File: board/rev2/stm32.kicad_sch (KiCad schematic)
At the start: 6 parts, among them U6 STM32G071CBUx

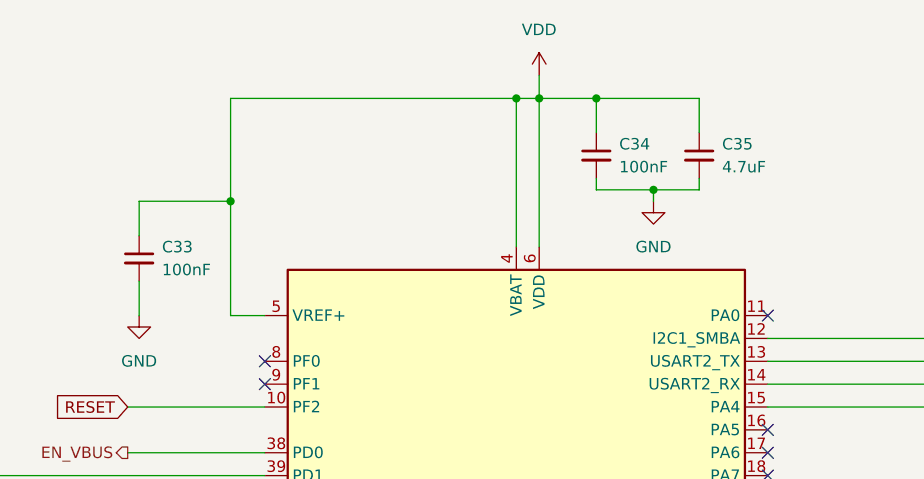
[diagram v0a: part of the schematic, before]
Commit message: Start board
add a few extra bypass caps too, and swap some pins on the USB mux

i forgot to add a bypass cap on the tpd6s so that also needs to happen

truly 63 capacitors is not enough
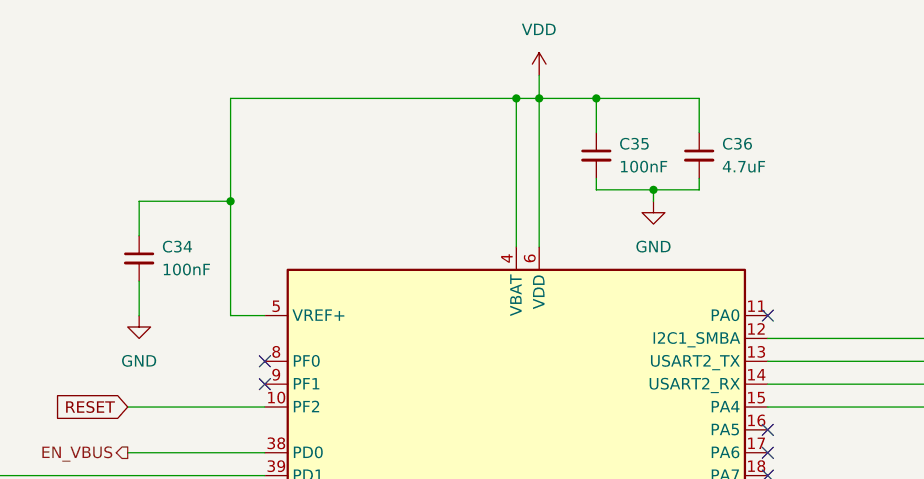
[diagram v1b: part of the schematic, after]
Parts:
- renumbered C33 to C34, C34 to C35, C35 to C36
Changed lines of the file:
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@@
 		(dnp no)
 		(fields_autoplaced yes)
-		(property "Reference" "C33"
+		(property "Reference" "C34"
 			(at 91.44 49.5362 0)
 			(effects
@@
 			(project ""
 				(path "/32eb05c7-b4a6-42f3-8fb3-43453631100f/4f7f35d0-2952-4294-913c-05f668985375"
-					(reference "C33")
+					(reference "C34")
 					(unit 1)
 				)
@@
 		(dnp no)
 		(fields_autoplaced yes)
-		(property "Reference" "C35"
+		(property "Reference" "C36"
 			(at 153.67 38.1062 0)
 			(effects
@@
 			(project ""
 				(path "/32eb05c7-b4a6-42f3-8fb3-43453631100f/4f7f35d0-2952-4294-913c-05f668985375"
-					(reference "C35")
+					(reference "C36")
 					(unit 1)
 				)
@@
 		(dnp no)
 		(fields_autoplaced yes)
-		(property "Reference" "C34"
+		(property "Reference" "C35"
 			(at 142.24 38.1062 0)
 			(effects
@@
 			(project ""
 				(path "/32eb05c7-b4a6-42f3-8fb3-43453631100f/4f7f35d0-2952-4294-913c-05f668985375"
-					(reference "C34")
-					(unit 1)
-				)
+					(reference "C35")
+					(unit 1)
+				)

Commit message: More tweaks to schematic, start laying out regulators
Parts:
- R11: footprint Resistor_SMD:R_0603_1608Metric -> Resistor_SMD:R_0402_1005Metric; LCSC C4184 -> C25765; Part 0603WAF2002T5E -> 0402WGF2002TCE
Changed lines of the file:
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@@
 			)
 		)
-		(property "Footprint" "Resistor_SMD:R_0603_1608Metric"
+		(property "Footprint" "Resistor_SMD:R_0402_1005Metric"
 			(at 54.61 78.74 0)
 			(effects
@@
 			)
 		)
-		(property "Part" "0603WAF2002T5E"
+		(property "Part" "0402WGF2002TCE"
 			(at 54.61 78.74 0)
 			(effects
@@
 			)
 		)
-		(property "LCSC" "C4184"
+		(property "LCSC" "C25765"
 			(at 54.61 78.74 0)
 			(effects

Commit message: Finish board rev2
woo another pcb
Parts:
- removed R11: 20k, Resistor_SMD:R_0402_1005Metric, symbol Device:R_Small_US
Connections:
- net ESP_RESET: no longer names the net of U6.39 (PD1)
- no-connect marks 19 -> 20

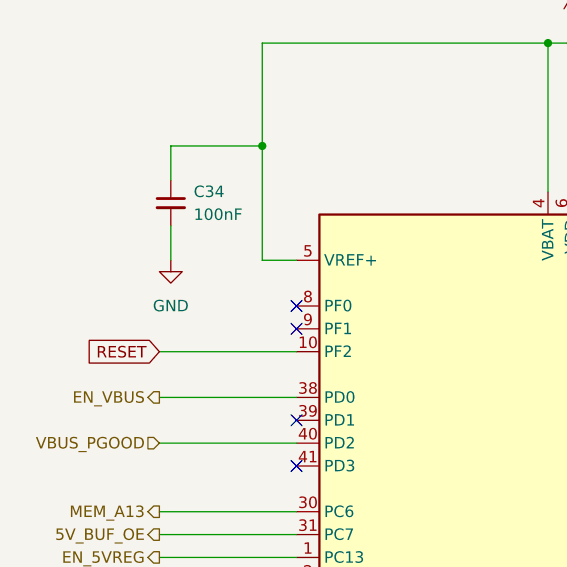
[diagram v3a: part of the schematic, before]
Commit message: Board REVB - fix 5V mux and add discharge path
also, fix a few routing issues
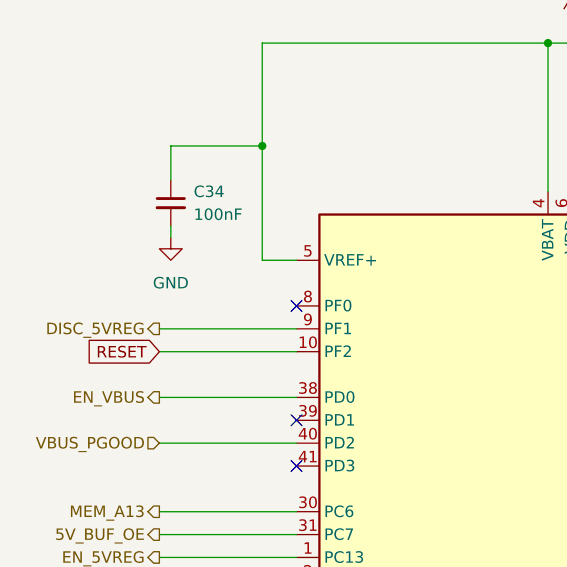
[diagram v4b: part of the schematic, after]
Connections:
- net DISC_5VREG: now reaches U6.9 (PF1)
- no-connect marks 20 -> 19
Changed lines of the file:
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@@
-	)
-	(no_connect
-		(at 102.87 64.77)
 	)
 	(no_connect
@@
 	)
 	(no_connect
+		(at 102.87 74.93)
+	)
+	(no_connect
 		(at 158.75 113.03)
 	)
@@
 	(no_connect
 		(at 158.75 105.41)
-	)
-	(no_connect
-		(at 102.87 74.93)
 	)
 	(no_connect
@@
 		)
 	)
+	(wire
+		(pts
+			(xy 87.63 64.77) (xy 102.87 64.77)
+		)
+		(stroke
+			(width 0)
+			(type default)
+		)
+	)
 	(bus
 		(pts
@@
 	(wire
 		(pts
-			(xy 88.9 53.34) (xy 88.9 57.15)
+			(xy 88.9 53.34) (xy 88.9 54.61)
 		)
 		(stroke
@@
 			)
 			(justify left)
+		)
+	)
+	(hierarchical_label "DISC_5VREG"
+		(shape output)
+		(at 87.63 64.77 180)
+		(effects
+			(font
+				(size 1.27 1.27)
+			)
+			(justify right)
 		)
 	)
@@
 	(symbol
 		(lib_id "power:GND")
-		(at 88.9 57.15 0)
+		(at 88.9 54.61 0)
 		(unit 1)
 		(body_style 1)
@@
 		(fields_autoplaced yes)
 		(property "Reference" "#PWR013"
-			(at 88.9 63.5 0)
+			(at 88.9 60.96 0)
 			(hide yes)
 			(show_name no)
@@
 		)
 		(property "Value" "GND"
-			(at 88.9 62.23 0)
+			(at 88.9 59.69 0)
 			(show_name no)
 			(do_not_autoplace no)
@@
 		)
 		(property "Footprint" ""
-			(at 88.9 57.15 0)
+			(at 88.9 54.61 0)
 			(hide yes)
 			(show_name no)
@@
 		)
 		(property "Datasheet" ""
-			(at 88.9 57.15 0)
+			(at 88.9 54.61 0)
 			(hide yes)
 			(show_name no)
@@
 		)
 		(property "Description" "Power symbol creates a global label with name \"GND\" , ground"
-			(at 88.9 57.15 0)
-			(hide yes)
-			(show_name no)
+			(at 88.9 54.61 0)
+			(hide yes)
+			(show_name no)
